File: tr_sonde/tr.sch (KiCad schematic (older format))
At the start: 90 parts, among them J1 SMA, J2 SMA, J3 SMA, K1 SMDHDR, K2 SMDHDR, K3 SMDHDR, Q3 STD2NK90ZT4, Q4 STD2NK90ZT4, U1 L6388E, U2 75451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

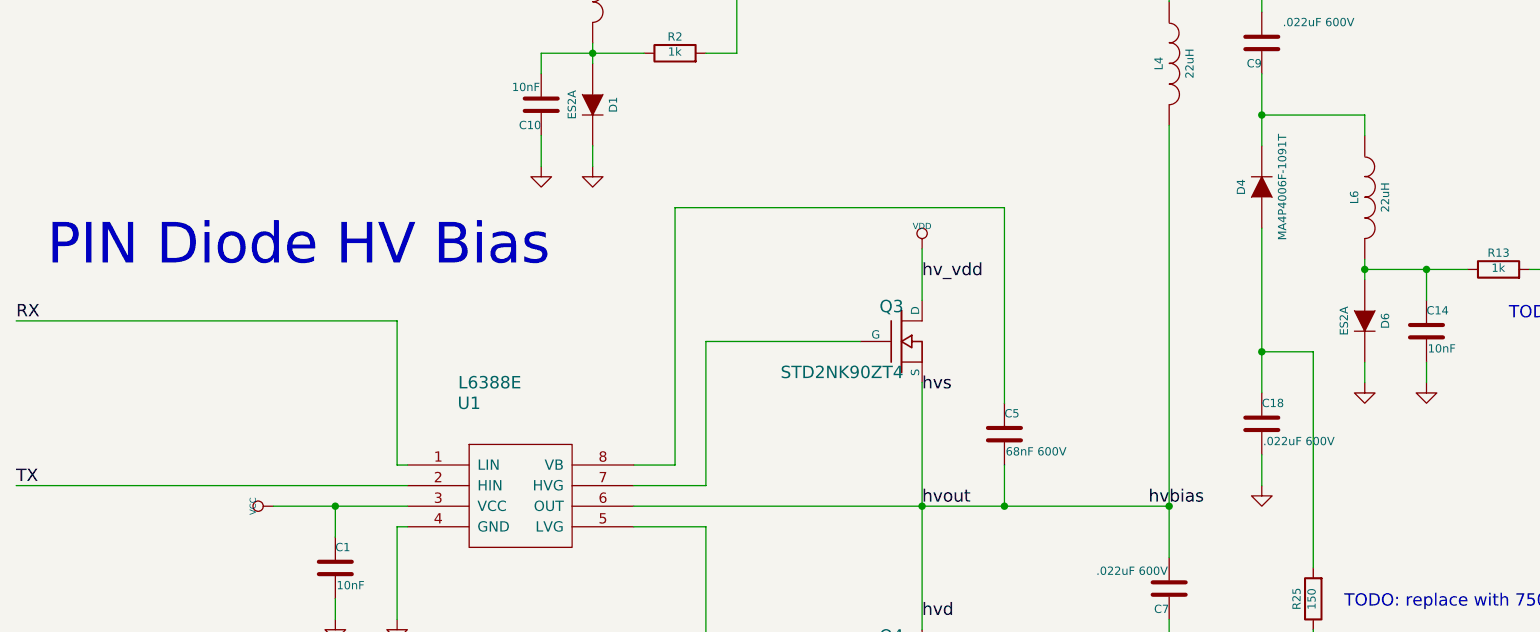
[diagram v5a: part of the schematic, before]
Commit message: updated agc to recent version of kicad - removed vestigial inner layers and fixed schematic for smaller passives
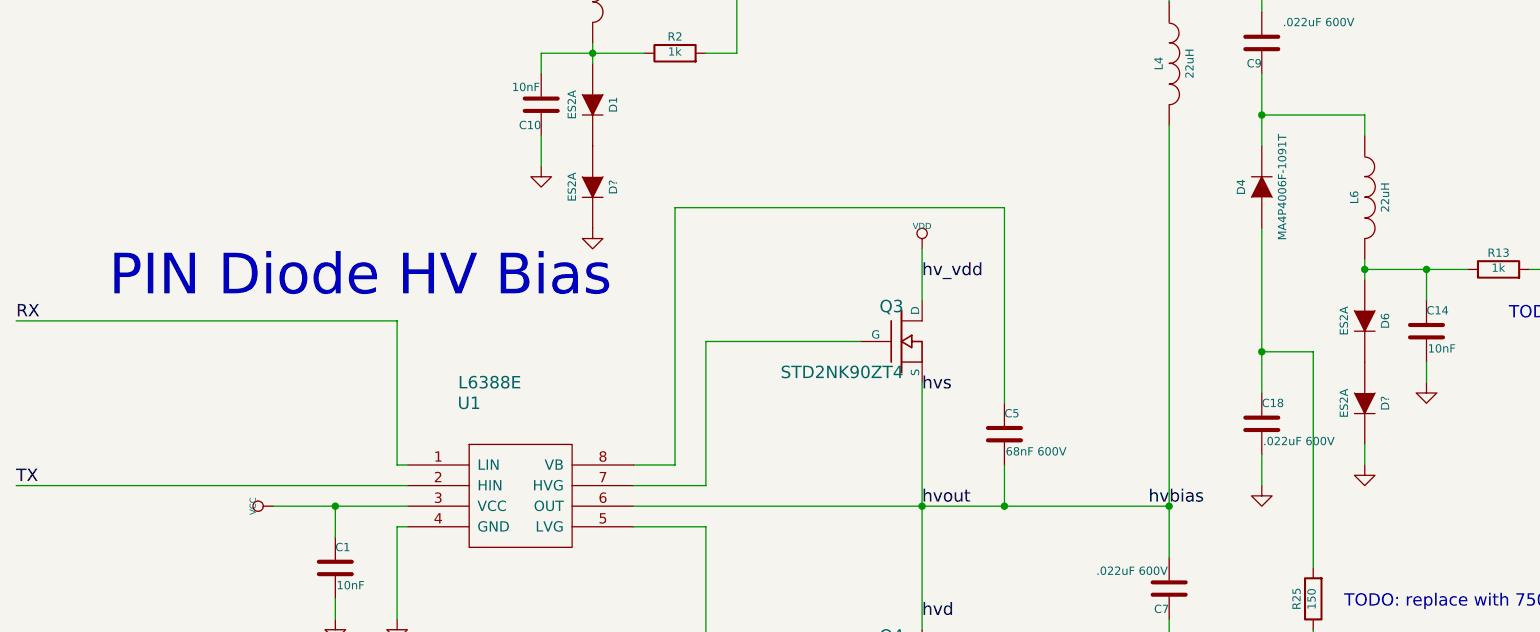
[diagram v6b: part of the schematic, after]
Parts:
- added D?: ES2A, SMD_Packages:DO-214-AA_SMB, symbol DIODE
- added D?: ES2A, smb_diode:SMB_DO2144AA, symbol DIODE
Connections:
- net GND: now also D?.2 (K), D?.2 (K); no longer D1.2 (K), D6.2 (K)
- new net: D1.2 (K), D?.1 (A)
- new net: D6.2 (K), D?.1 (A)
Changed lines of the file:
@@
 L GND #PWR012
 U 1 1 52ABB85F
-P 3350 7200
-F 0 "#PWR012" H 3350 7200 30  0001 C CNN
-F 1 "GND" H 3350 7130 30  0001 C CNN
-F 2 "" H 3350 7200 60  0000 C CNN
-F 3 "" H 3350 7200 60  0000 C CNN
-	1    3350 7200
+P 3350 7500
+F 0 "#PWR012" H 3350 7500 30  0001 C CNN
+F 1 "GND" H 3350 7430 30  0001 C CNN
+F 2 "" H 3350 7500 60  0000 C CNN
+F 3 "" H 3350 7500 60  0000 C CNN
+	1    3350 7500
 	1    0    0    -1
 $EndComp
@@
 L GND #PWR013
 U 1 1 52ABBCDA
-P 7100 8250
-F 0 "#PWR013" H 7100 8250 30  0001 C CNN
-F 1 "GND" H 7100 8180 30  0001 C CNN
-F 2 "" H 7100 8250 60  0000 C CNN
-F 3 "" H 7100 8250 60  0000 C CNN
-	1    7100 8250
+P 7100 8650
+F 0 "#PWR013" H 7100 8650 30  0001 C CNN
+F 1 "GND" H 7100 8580 30  0001 C CNN
+F 2 "" H 7100 8650 60  0000 C CNN
+F 3 "" H 7100 8650 60  0000 C CNN
+	1    7100 8650
 	1    0    0    -1
 $EndComp
@@
 Text Notes 9450 7000 0    197  ~ 0
 PIN Diode Current Driver
-Text Notes 700  7700 0    197  ~ 0
+Text Notes 1000 7850 0    197  ~ 0
 PIN Diode HV Bias
 Text Notes 3750 1300 0    197  ~ 0
@@
 	7100 7650 7100 7750
 Wire Wire Line
-	7100 8150 7100 8250
+	7100 8550 7100 8650
 Wire Wire Line
 	4050 6650 4050 6350
@@
 Wire Wire Line
 	3350 6600 3350 6700
-Wire Wire Line
-	3350 7100 3350 7200
 Wire Wire Line
 	6150 7000 6150 9100
@@
 TODO: replace with 500ish ohms\n
 Connection ~ 4250 5800
+$Comp
+L DIODE D?
+U 1 1 551138AC
+P 7100 8350
+F 0 "D?" H 7100 8450 40  0000 C CNN
+F 1 "ES2A" H 7100 8250 40  0000 C CNN
+F 2 "SMD_Packages:DO-214-AA_SMB" H 7100 8350 60  0001 C CNN
+F 3 "~" H 7100 8350 60  0000 C CNN
+F 4 "FAIRCHILD SEMICONDUCTOR (VA)" H 7100 8350 60  0001 C CNN "MFG Name"
+F 5 "ES2B" H 7100 8350 60  0001 C CNN "MFG PN"
+F 6 "DigiKey" H 7100 8350 60  0001 C CNN "Dist Name"
+F 7 "ES2BFSDKR-ND" H 7100 8350 60  0001 C CNN "Dist PN"
+	1    7100 8350
+	0    1    1    0
+$EndComp
+$Comp
+L DIODE D?
+U 1 1 551165AA
+P 3350 7300
+F 0 "D?" H 3350 7400 40  0000 C CNN
+F 1 "ES2A" H 3350 7200 40  0000 C CNN
+F 2 "smb_diode:SMB_DO2144AA" H 3350 7300 60  0001 C CNN
+F 3 "~" H 3350 7300 60  0000 C CNN
+F 4 "FAIRCHILD SEMICONDUCTOR (VA)" H 3350 7300 60  0001 C CNN "MFG Name"
+F 5 "ES2B" H 3350 7300 60  0001 C CNN "MFG PN"
+F 6 "DigiKey" H 3350 7300 60  0001 C CNN "Dist Name"
+F 7 "ES2BFSDKR-ND" H 3350 7300 60  0001 C CNN "Dist PN"
+	1    3350 7300
+	0    1    1    0
+$EndComp
 $EndSCHEMATC

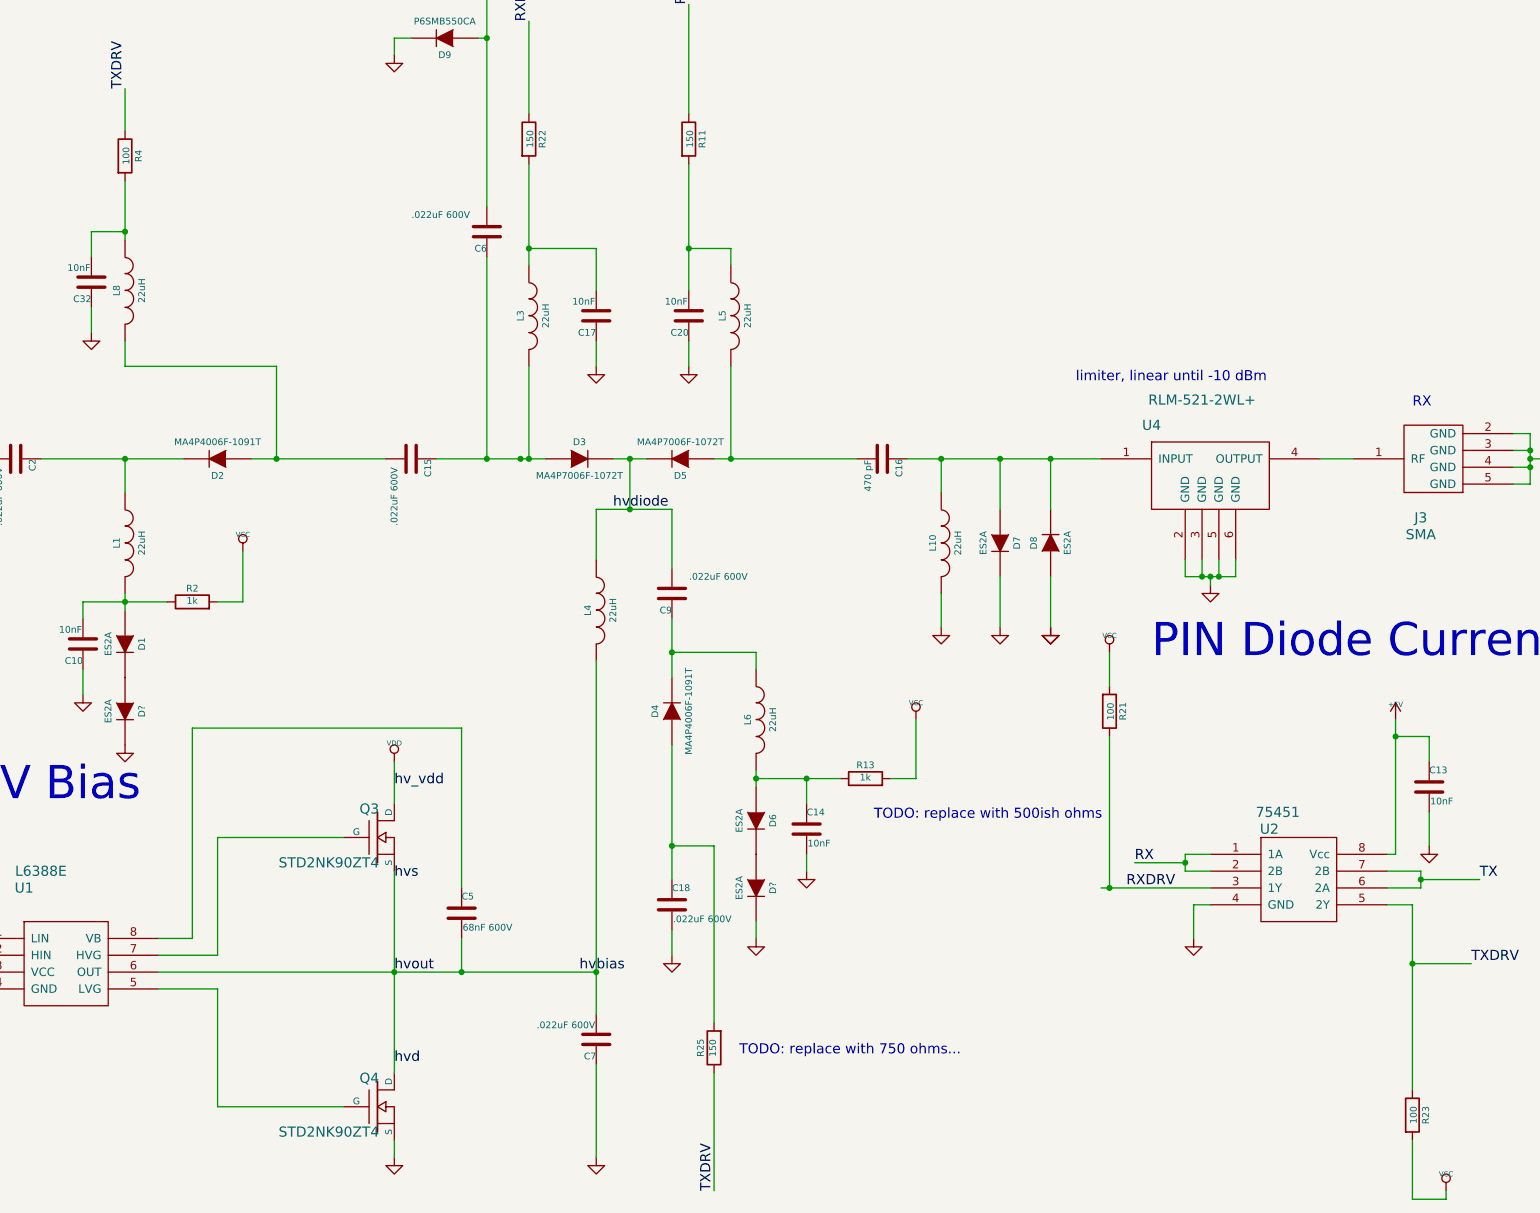
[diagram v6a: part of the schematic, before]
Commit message: modified hptr for higher power resistors
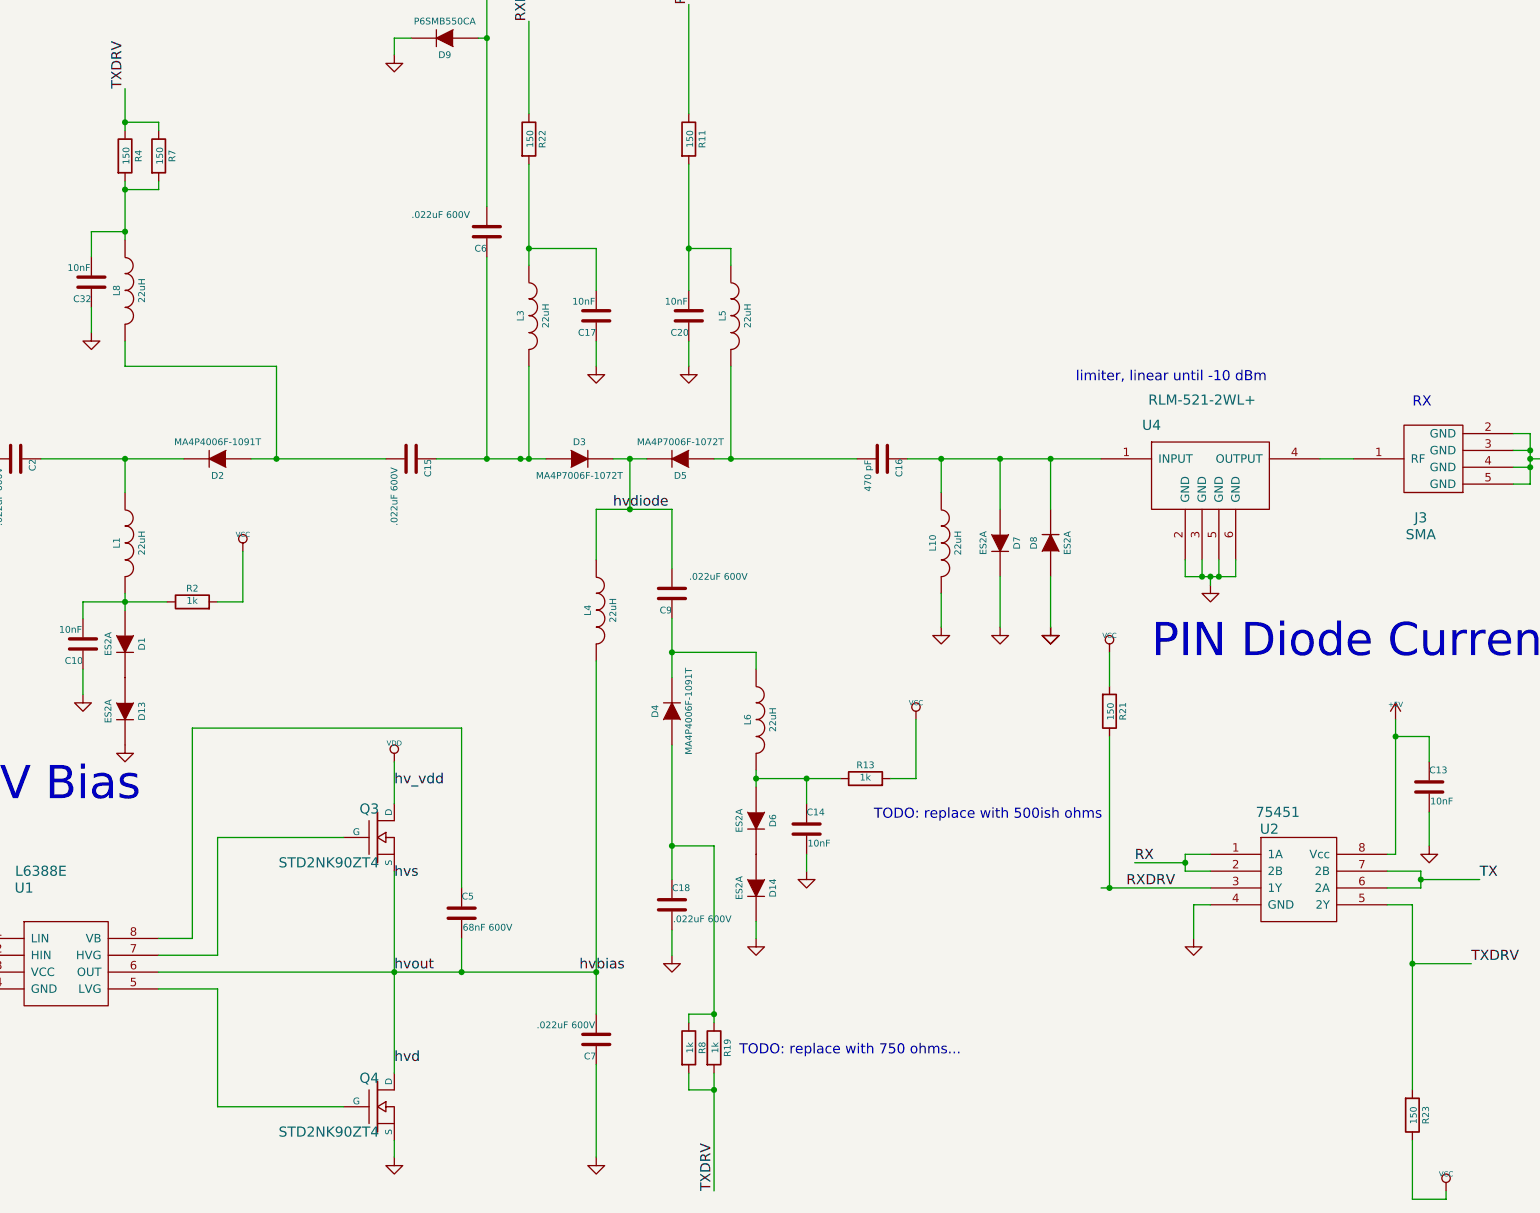
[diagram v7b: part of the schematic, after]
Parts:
- removed D?: ES2A, smb_diode:SMB_DO2144AA, symbol DIODE
- removed R25: 150, smd_capacitors:c_1210, symbol R
- added D13: ES2A, SMD_Packages:DO-214-AA_SMB, symbol DIODE
- added R19, R8: 1k, smd_capacitors:c_0805, symbol R
- added R7: 150, smd_capacitors:c_1210, symbol R
- D1, D12: footprint smb_diode:SMB_DO2144AA -> SMD_Packages:DO-214-AA_SMB
- R21, R23: value 100 -> 150; footprint smd_capacitors:c_1210 -> Resistors_SMD:R_2512; Dist PN P100VDKR-ND -> A116012DKR-ND; MFG Name PANASONIC ELECTRONIC COMPONENTS (VA) -> TE Connectivity; MFG PN ERJ-14YJ101U -> 2-2176070-9
- R4: value 100 -> 150; Dist PN P100VDKR-ND -> P150VDKR-ND; MFG PN ERJ-14YJ101U -> ERJ-14YJ151U
- gave numbers to parts that had none: 1
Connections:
- net GND: now also D13.2 (K)
- net TXDRV: now also R23.2, R19.2, R7.1, R8.2; no longer R23.1
- net VCC: now also R23.1; no longer R23.2
- net at C18.1, D4.1 (A): now also R19.1, R8.1
- net at D1.2 (K): now also D13.1 (A)
- net at C32.2, L8.1, R4.2: now also R7.2
